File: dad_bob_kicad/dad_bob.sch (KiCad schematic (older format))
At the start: 66 parts, among them J1 Conn_01x01, J10 Conn_01x03_Male, J12 USB4085-GF-A_REVA4, J13 Conn_01x03_Male, J14 Conn_01x03_Male, J2 Conn_01x01, J3 Conn_01x01, J4 Conn_01x01, J5 Conn_01x03_Male, J6 Conn_02x15_Odd_Even, J7 BNC5-J-P-GN-RA-BH2D, J8 Conn_01x03_Male, J9 Conn_02x15_Odd_Even, K1 EC2-5NU, K2 EC2-5NU, Q1 2N3904, Q2 2N3904, T1 GT07-110-013, U1 SL1002A600SP

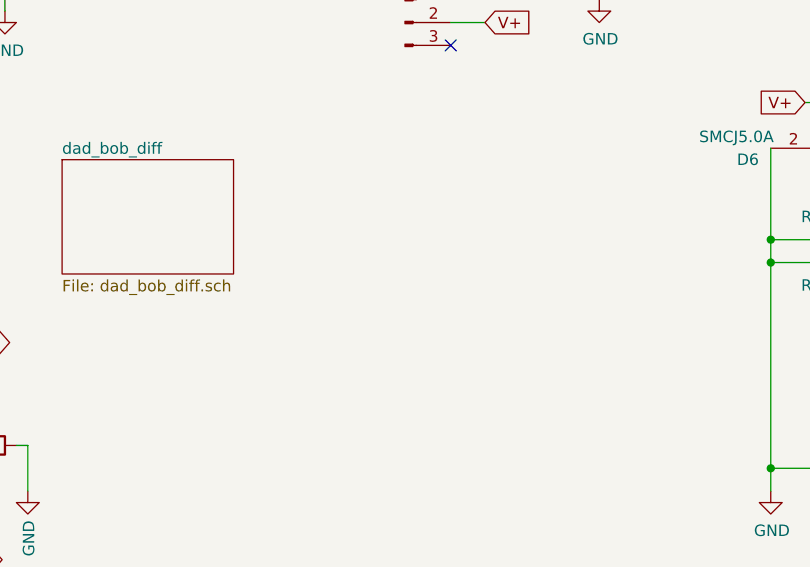
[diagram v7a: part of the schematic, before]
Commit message: End of day, layout reworked. Mostly ready to route
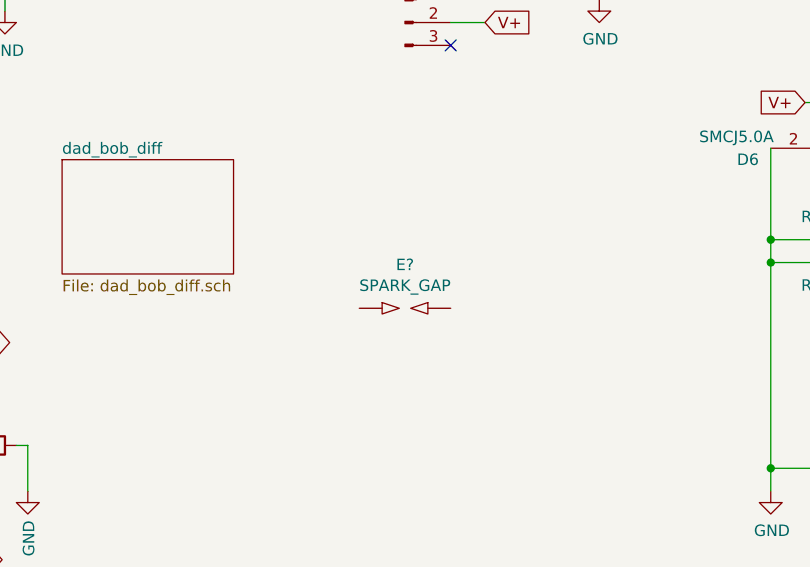
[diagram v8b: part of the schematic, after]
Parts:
- added E?: SPARK_GAP, symbol Device:SPARK_GAP
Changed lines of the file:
@@
 Wire Wire Line
 	6400 4200 6250 4200
+$Comp
+L Device:SPARK_GAP E?
+U 1 1 62690EA2
+P 6050 5450
+F 0 "E?" H 6050 5640 50  0000 C CNN
+F 1 "SPARK_GAP" H 6050 5549 50  0000 C CNN
+F 2 "" H 6050 5380 50  0001 C CNN
+F 3 "~" V 6050 5450 50  0001 C CNN
+	1    6050 5450
+	1    0    0    -1
+$EndComp
 $EndSCHEMATC
